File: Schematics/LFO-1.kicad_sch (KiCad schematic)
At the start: 54 parts, among them J49 Conn_01x10h, J50 Conn_01x03, J51 Conn_01x04, J52 Conn_01x04, U100 LM78L05, U101 SSI2130, U102 LM324, U103 LM324, U99 LM324

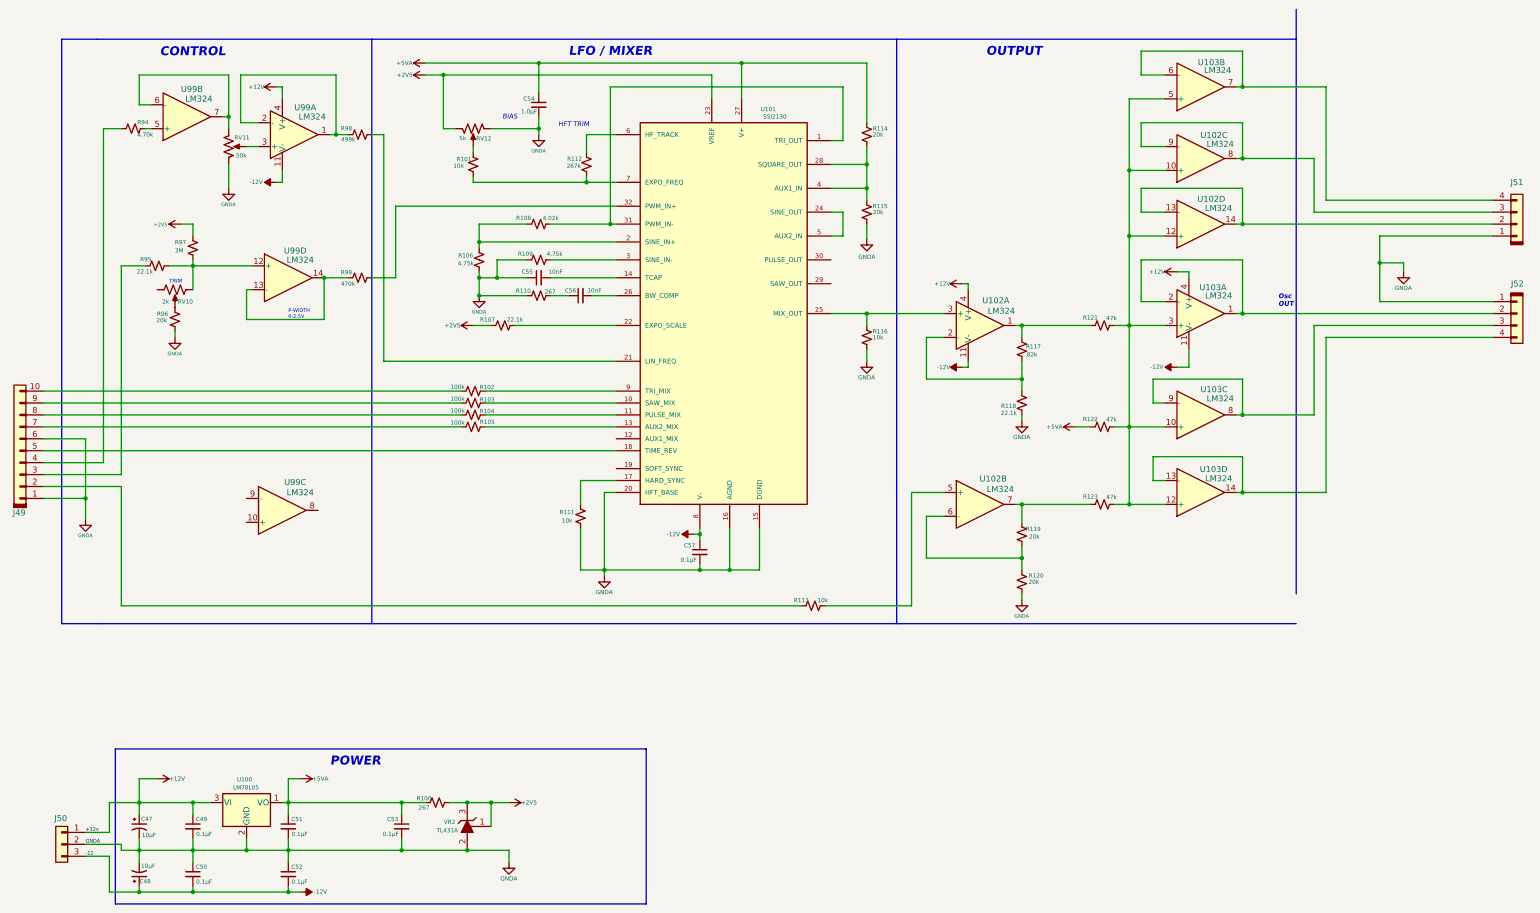
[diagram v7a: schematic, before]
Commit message: Partial software with complete hardware on best 3 state filter with 4 outputs.
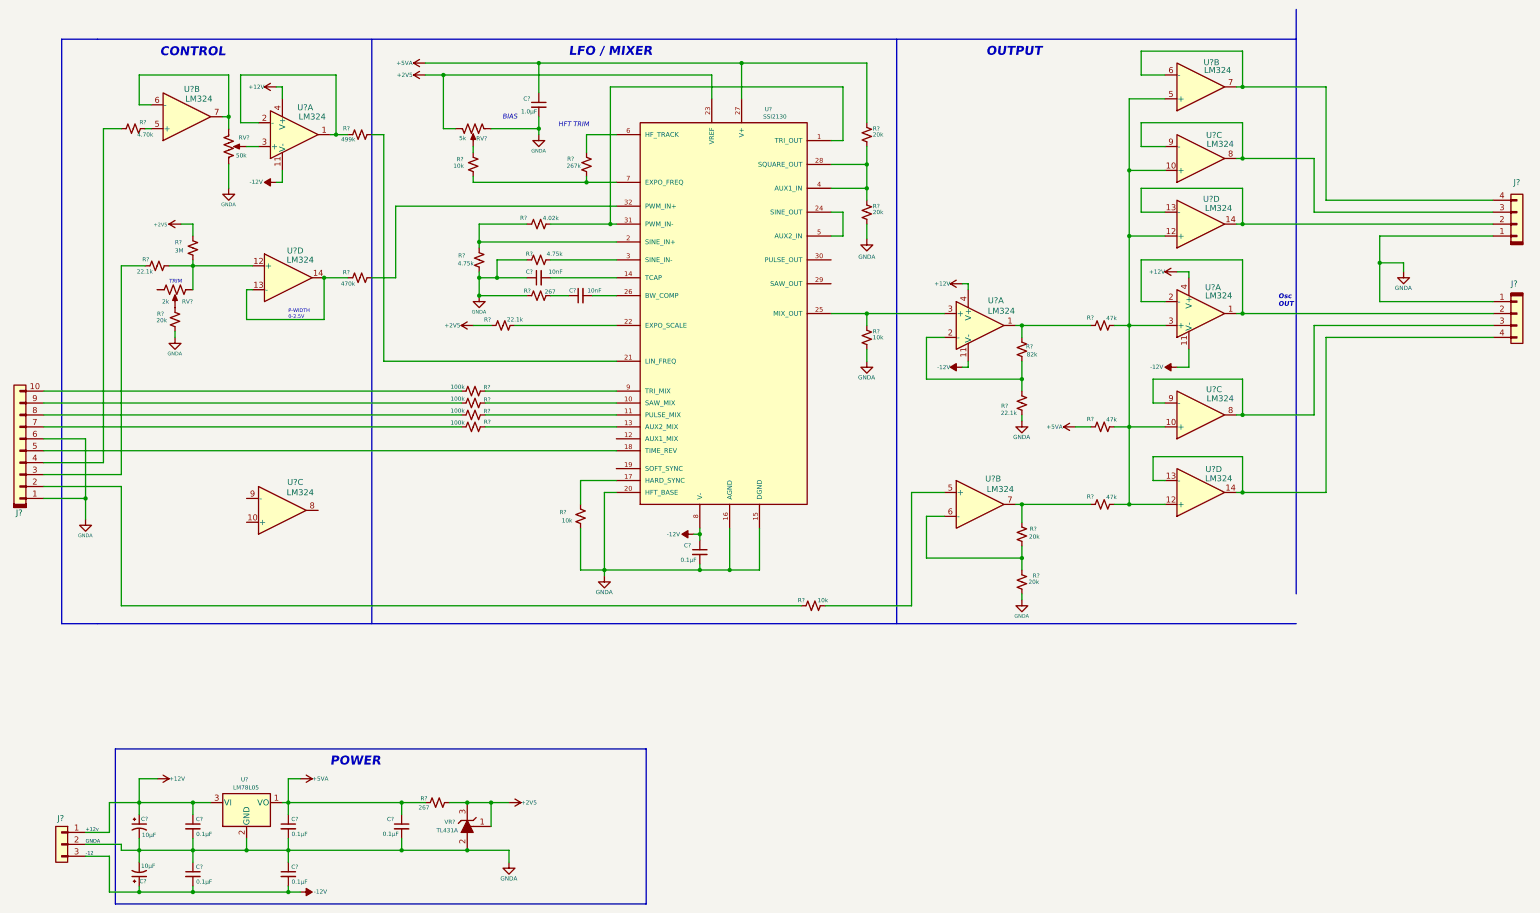
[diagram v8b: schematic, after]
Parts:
- renumbered C57 to C?, C47 to C?, C55 to C?, C49 to C?, C52 to C?, C56 to C?, C48 to C?, C50 to C?, C51 to C?, C53 to C?, C54 to C?, J49 to J?, J50 to J?, J52 to J?, J51 to J?, R115 to R?, R107 to R?, R95 to R?, R94 to R?, R120 to R?, R100 to R?, R99 to R?, R97 to R?, R106 to R?, R112 to R?, R119 to R?, R123 to R?, R114 to R?, R103 to R?, R111 to R?, R117 to R?, R102 to R?, R121 to R?, R116 to R?, R122 to R?, R96 to R?, R109 to R?, R105 to R?, R108 to R?, R113 to R?, R118 to R?, R104 to R?, R98 to R?, R101 to R?, R110 to R?, RV10 to RV?, RV11 to RV?, RV12 to RV?, U99 to U?, U103 to U?, U102 to U?, U100 to U?, U101 to U?, VR2 to VR?
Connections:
- net at RV?. (3): now also R?.1
